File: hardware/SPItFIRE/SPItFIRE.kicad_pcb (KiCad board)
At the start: 2 copper layers, 114.3 x 83.8 mm, 45 parts, among them J1 Compact Host, J10 ISP, J11 Joystick A, J12 Joystick B, J13 Peripheral DE-9, J14 Peripheral User Port, J2 User Port Host, J3 User Port Passthrough, J4 SD Card Adapter, J5 DeadOnRTC, J6 SPI_4, J7 SPI_5, J8 SPI_6, J9 SPI_7, U1 74HC138, U2 ATmega1284P-A, Y1 Crystal

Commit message: Crystal load capacitors C2 and C6 are 0201 instead of 0603 and were missing their 27 pF values in the schematic
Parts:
- C2, C6: footprint Capacitor_SMD:C_0201_0603Metric_Pad0.64x0.40mm_HandSolder -> Capacitor_SMD:C_0603_1608Metric_Pad1.08x0.95mm_HandSolder
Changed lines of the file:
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@@
 		)
 	)
-	(footprint "Capacitor_SMD:C_0201_0603Metric_Pad0.64x0.40mm_HandSolder"
+	(footprint "Capacitor_SMD:C_0603_1608Metric_Pad1.08x0.95mm_HandSolder"
 		(layer "F.Cu")
 		(at 121.285 90.17)
-		(descr "Capacitor SMD 0201 (0603 Metric), square (rectangular) end terminal, IPC-7351 nominal with elongated pad for handsoldering. (Body size source: https://www.vishay.com/docs/20052/crcw0201e3.pdf)")
+		(descr "Capacitor SMD 0603 (1608 Metric), square (rectangular) end terminal, IPC-7351 nominal with elongated pad for handsoldering. (Body size source: IPC-SM-782 page 76, https://www.pcb-3d.com/wordpress/wp-content/uploads/ipc-sm-782a_amendment_1_and_2.pdf)")
 		(tags "capacitor handsolder")
 		(property "Reference" "C6"
-			(at 0 -1.05 0)
+			(at 2.667 0 0)
 			(layer "F.SilkS")
 			(effects
@@
 		)
 		(property "Value" "27pF"
-			(at 0 1.05 0)
+			(at 0 1.43 0)
 			(layer "F.Fab")
 			(effects
@@
 		(attr smd)
 		(duplicate_pad_numbers_are_jumpers no)
+		(fp_line
+			(start -0.146267 -0.51)
+			(end 0.146267 -0.51)
+			(stroke
+				(width 0.12)
+				(type solid)
+			)
+			(layer "F.SilkS")
+		)
+		(fp_line
+			(start -0.146267 0.51)
+			(end 0.146267 0.51)
+			(stroke
+				(width 0.12)
+				(type solid)
+			)
+			(layer "F.SilkS")
+		)
 		(fp_rect
-			(start -0.88 -0.35)
-			(end 0.88 0.35)
+			(start -1.65 -0.73)
+			(end 1.65 0.73)
 			(stroke
 				(width 0.05)
@@
 		)
 		(fp_rect
-			(start -0.3 -0.15)
-			(end 0.3 0.15)
+			(start -0.8 -0.4)
+			(end 0.8 0.4)
 			(stroke
 				(width 0.1)
@@
 		)
 		(fp_text user "${REFERENCE}"
-			(at 0 -0.68 0)
+			(at 0 0 0)
 			(layer "F.Fab")
 			(effects
 				(font
-					(size 0.25 0.25)
-					(thickness 0.04)
+					(size 0.4 0.4)
+					(thickness 0.06)
 				)
 			)
 		)
-		(pad "" smd roundrect
-			(at -0.4325 0)
-			(size 0.458 0.36)
-			(layers "F.Paste")
-			(roundrect_rratio 0.25)
-		)
-		(pad "" smd roundrect
-			(at 0.4325 0)
-			(size 0.458 0.36)
-			(layers "F.Paste")
-			(roundrect_rratio 0.25)
-		)
 		(pad "1" smd roundrect
-			(at -0.4075 0)
-			(size 0.635 0.4)
-			(layers "F.Cu" "F.Mask")
+			(at -0.8625 0)
+			(size 1.075 0.95)
+			(layers "F.Cu" "F.Mask" "F.Paste")
 			(roundrect_rratio 0.25)
 			(net "Net-(U2A-XTAL2)")
@@
 		)
 		(pad "2" smd roundrect
-			(at 0.4075 0)
-			(size 0.635 0.4)
-			(layers "F.Cu" "F.Mask")
+			(at 0.8625 0)
+			(size 1.075 0.95)
+			(layers "F.Cu" "F.Mask" "F.Paste")
 			(roundrect_rratio 0.25)
 			(net "GND")
@@
 		)
 		(embedded_fonts no)
-		(model "${KICAD10_3DMODEL_DIR}/Capacitor_SMD.3dshapes/C_0201_0603Metric.step"
+		(model "${KICAD10_3DMODEL_DIR}/Capacitor_SMD.3dshapes/C_0603_1608Metric.step"
 			(offset
 				(xyz 0 0 0)
@@
 		(tags "Through hole horizontal IDC header THT 2x10 2.54mm double row")
 		(property "Reference" "J14"
-			(at 7.145 -11.97 0)
+			(at -2.921 -10.414 0)
 			(layer "F.SilkS")
 			(effects
@@
 		)
 	)
-	(footprint "Capacitor_SMD:C_0201_0603Metric_Pad0.64x0.40mm_HandSolder"
+	(footprint "Capacitor_SMD:C_0603_1608Metric_Pad1.08x0.95mm_HandSolder"
 		(layer "F.Cu")
 		(at 121.285 97.79 180)
-		(descr "Capacitor SMD 0201 (0603 Metric), square (rectangular) end terminal, IPC-7351 nominal with elongated pad for handsoldering. (Body size source: https://www.vishay.com/docs/20052/crcw0201e3.pdf)")
+		(descr "Capacitor SMD 0603 (1608 Metric), square (rectangular) end terminal, IPC-7351 nominal with elongated pad for handsoldering. (Body size source: IPC-SM-782 page 76, https://www.pcb-3d.com/wordpress/wp-content/uploads/ipc-sm-782a_amendment_1_and_2.pdf)")
 		(tags "capacitor handsolder")
 		(property "Reference" "C2"
-			(at 0 -1.05 180)
+			(at 0 -1.43 180)
 			(layer "F.SilkS")
 			(effects
@@
 		)
 		(property "Value" "27pF"
-			(at 0 1.05 180)
+			(at 0 1.43 180)
 			(layer "F.Fab")
 			(effects
@@
 		(attr smd)
 		(duplicate_pad_numbers_are_jumpers no)
+		(fp_line
+			(start -0.146267 0.51)
+			(end 0.146267 0.51)
+			(stroke
+				(width 0.12)
+				(type solid)
+			)
+			(layer "F.SilkS")
+		)
+		(fp_line
+			(start -0.146267 -0.51)
+			(end 0.146267 -0.51)
+			(stroke
+				(width 0.12)
+				(type solid)
+			)
+			(layer "F.SilkS")
+		)
 		(fp_rect
-			(start -0.88 -0.35)
-			(end 0.88 0.35)
+			(start -1.65 -0.73)
+			(end 1.65 0.73)
 			(stroke
 				(width 0.05)
@@
 		)
 		(fp_rect
-			(start -0.3 -0.15)
-			(end 0.3 0.15)
+			(start -0.8 -0.4)
+			(end 0.8 0.4)
 			(stroke
 				(width 0.1)
@@
 		)
 		(fp_text user "${REFERENCE}"
-			(at 0 -0.68 180)
+			(at 0 0 180)
 			(layer "F.Fab")
 			(effects
 				(font
-					(size 0.25 0.25)
-					(thickness 0.04)
+					(size 0.4 0.4)
+					(thickness 0.06)
 				)
 			)
 		)
-		(pad "" smd roundrect
-			(at -0.4325 0 180)
-			(size 0.458 0.36)
-			(layers "F.Paste")
-			(roundrect_rratio 0.25)
-		)
-		(pad "" smd roundrect
-			(at 0.4325 0 180)
-			(size 0.458 0.36)
-			(layers "F.Paste")
-			(roundrect_rratio 0.25)
-		)
 		(pad "1" smd roundrect
-			(at -0.4075 0 180)
-			(size 0.635 0.4)
-			(layers "F.Cu" "F.Mask")
+			(at -0.8625 0 180)
+			(size 1.075 0.95)
+			(layers "F.Cu" "F.Mask" "F.Paste")
 			(roundrect_rratio 0.25)
 			(net "Net-(U2A-XTAL1)")
@@
 		)
 		(pad "2" smd roundrect
-			(at 0.4075 0 180)
-			(size 0.635 0.4)
-			(layers "F.Cu" "F.Mask")
+			(at 0.8625 0 180)
+			(size 1.075 0.95)
+			(layers "F.Cu" "F.Mask" "F.Paste")
 			(roundrect_rratio 0.25)
 			(net "GND")
@@
 		)
 		(embedded_fonts no)
-		(model "${KICAD10_3DMODEL_DIR}/Capacitor_SMD.3dshapes/C_0201_0603Metric.step"
+		(model "${KICAD10_3DMODEL_DIR}/Capacitor_SMD.3dshapes/C_0603_1608Metric.step"
 			(offset
 				(xyz 0 0 0)
@@
 		(tags "resistor handsolder")
 		(property "Reference" "R2"
-			(at 0 1.397 270)
+			(at 0 1.905 0)
 			(layer "F.SilkS")
 			(effects
@@
 		(tags "capacitor handsolder")
 		(property "Reference" "C5"
-			(at 2.54 -1.27 0)
+			(at 2.413 -0.127 90)
 			(layer "F.SilkS")
 			(effects
@@
 	)
 	(segment
+		(start 122.1475 89.99)
+		(end 120.4225 88.265)
+		(width 0.2)
+		(layer "F.Cu")
+		(net "GND")
+	)
+	(segment
 		(start 168.91 78.74)
 		(end 162.56 78.74)
@@
 	)
 	(segment
+		(start 122.1475 90.17)
+		(end 122.1475 89.99)
+		(width 0.2)
+		(layer "F.Cu")
+		(net "GND")
+	)
+	(segment
 		(start 130.175 53.34)
 		(end 154.94 53.34)
@@
 	)
 	(segment
-		(start 120.4225 89.3075)
-		(end 120.65 89.535)
-		(width 0.2)
-		(layer "F.Cu")
-		(net "GND")
-	)
-	(segment
 		(start 140.97 58.42)
 		(end 139.7 57.15)
@@
 	)
 	(segment
-		(start 121.6925 89.9425)
-		(end 121.285 89.535)
-		(width 0.2)
-		(layer "F.Cu")
-		(net "GND")
-	)
-	(segment
 		(start 74.93 105.41)
 		(end 76.2 106.68)
@@
 	)
 	(segment
-		(start 120.4225 88.265)
-		(end 120.4225 89.3075)
-		(width 0.2)
-		(layer "F.Cu")
-		(net "GND")
-	)
-	(segment
 		(start 142.24 68.58)
 		(end 142.24 64.320635)
@@
 		(width 0.2)
 		(layer "F.Cu")
-		(net "GND")
-	)
-	(segment
-		(start 121.285 89.535)
-		(end 120.65 89.535)
-		(width 0.2)
-		(layer "F.Cu")

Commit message: Adds weak pull-ups to the address lines to give them definite state when the Compact is not connected
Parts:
- added R10: 100K, Resistor_SMD:R_0603_1608Metric_Pad0.98x0.95mm_HandSolder, F.Cu at (82.3, 59.2)
- added R8: 100K, Resistor_SMD:R_0603_1608Metric_Pad0.98x0.95mm_HandSolder, F.Cu at (78.0, 59.2)
- added R9: 100K, Resistor_SMD:R_0603_1608Metric_Pad0.98x0.95mm_HandSolder, F.Cu at (86.9, 59.2)
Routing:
- net +5V: track 574.2 -> 596.6 mm
- net /main/A2: track 90.0 -> 105.0 mm, vias 1 -> 2
- net GND: track 827.5 -> 820.2 mm
- net /main/A1: track 80.8 -> 84.5 mm
- net /main/A0: track 86.0 -> 89.2 mm
- net SCK: track 291.0 -> 292.5 mm

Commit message: Fixed the footprint of C3
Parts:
- C3: footprint LED_SMD:LED_0603_1608Metric_Pad1.05x0.95mm_HandSolder -> Capacitor_SMD:C_0603_1608Metric_Pad1.08x0.95mm_HandSolder
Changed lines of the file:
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@@
 		)
 	)
-	(footprint "LED_SMD:LED_0603_1608Metric_Pad1.05x0.95mm_HandSolder"
+	(footprint "Capacitor_SMD:C_0603_1608Metric_Pad1.08x0.95mm_HandSolder"
 		(layer "F.Cu")
 		(at 132.715 80.645 180)
-		(descr "LED SMD 0603 (1608 Metric), square (rectangular) end terminal, IPC-7351 nominal, (Body size source: http://www.tortai-tech.com/upload/download/2011102023233369053.pdf)")
-		(tags "LED handsolder")
+		(descr "Capacitor SMD 0603 (1608 Metric), square (rectangular) end terminal, IPC-7351 nominal with elongated pad for handsoldering. (Body size source: IPC-SM-782 page 76, https://www.pcb-3d.com/wordpress/wp-content/uploads/ipc-sm-782a_amendment_1_and_2.pdf)")
+		(tags "capacitor handsolder")
 		(property "Reference" "C3"
-			(at 0 1.905 0)
+			(at -0.033767 1.397 180)
 			(layer "F.SilkS")
 			(effects
@@
 		)
 		(property "Value" "10uF"
-			(at -3.81 0 0)
+			(at 0 1.43 180)
 			(layer "F.Fab")
 			(effects
@@
 		)
 		(property "Datasheet" ""
-			(at 0 0 0)
+			(at 0 0 180)
 			(layer "F.Fab")
 			(hide yes)
@@
 		)
 		(property "Description" "Unpolarized capacitor"
-			(at 0 0 0)
+			(at 0 0 180)
 			(layer "F.Fab")
 			(hide yes)
@@
 		)
 		(property "KiLib_Generator" "SMD_2terminal_chip_molded"
-			(at 0 0 0)
+			(at 0 0 180)
 			(layer "F.SilkS")
 			(hide yes)
@@
 		(duplicate_pad_numbers_are_jumpers no)
 		(fp_line
-			(start 0.8 -0.735)
-			(end -1.66 -0.735)
-			(stroke
-				(width 0.12)
-				(type solid)
-			)
-			(layer "F.SilkS")
-		)
-		(fp_line
-			(start -1.66 0.735)
-			(end 0.8 0.735)
+			(start -0.146267 0.51)
+			(end 0.146267 0.51)
 			(stroke
 				(width 0.12)
@@
 		)
 		(fp_line
-			(start -1.66 -0.735)
-			(end -1.66 0.735)
+			(start -0.146267 -0.51)
+			(end 0.146267 -0.51)
 			(stroke
 				(width 0.12)
@@
 			(layer "F.CrtYd")
 		)
-		(fp_line
-			(start 0.8 0.4)
-			(end 0.8 -0.4)
-			(stroke
-				(width 0.1)
-				(type solid)
-			)
-			(layer "F.Fab")
-		)
-		(fp_line
-			(start 0.8 -0.4)
-			(end -0.5 -0.4)
-			(stroke
-				(width 0.1)
-				(type solid)
-			)
-			(layer "F.Fab")
-		)
-		(fp_line
-			(start -0.5 -0.4)
-			(end -0.8 -0.1)
-			(stroke
-				(width 0.1)
-				(type solid)
-			)
-			(layer "F.Fab")
-		)
-		(fp_line
-			(start -0.8 0.4)
+		(fp_rect
+			(start -0.8 -0.4)
 			(end 0.8 0.4)
 			(stroke
@@
 				(type solid)
 			)
-			(layer "F.Fab")
-		)
-		(fp_line
-			(start -0.8 -0.1)
-			(end -0.8 0.4)
-			(stroke
-				(width 0.1)
-				(type solid)
-			)
+			(fill no)
 			(layer "F.Fab")
 		)
 		(fp_text user "${REFERENCE}"
-			(at 0 0 0)
+			(at 0 0 180)
 			(layer "F.Fab")
 			(effects
@@
 		)
 		(pad "1" smd roundrect
-			(at -0.875 0 180)
-			(size 1.05 0.95)
+			(at -0.8625 0 180)
+			(size 1.075 0.95)
 			(layers "F.Cu" "F.Mask" "F.Paste")
 			(roundrect_rratio 0.25)
@@
 		)
 		(pad "2" smd roundrect
-			(at 0.875 0 180)
-			(size 1.05 0.95)
+			(at 0.8625 0 180)
+			(size 1.075 0.95)
 			(layers "F.Cu" "F.Mask" "F.Paste")
 			(roundrect_rratio 0.25)
@@
 		)
 		(embedded_fonts no)
-		(model "${KICAD10_3DMODEL_DIR}/LED_SMD.3dshapes/LED_0603_1608Metric.step"
+		(model "${KICAD10_3DMODEL_DIR}/Capacitor_SMD.3dshapes/C_0603_1608Metric.step"
 			(offset
 				(xyz 0 0 0)
@@
 		(tags "resistor handsolder")
 		(property "Reference" "R1"
-			(at 0 -1.43 90)
+			(at 2.4395 0.127 180)
 			(layer "F.SilkS")
 			(effects
@@
 		(tags "capacitor handsolder")
 		(property "Reference" "C4"
-			(at -2.3125 0 180)
+			(at -2.4395 0 180)
 			(layer "F.SilkS")
 			(effects

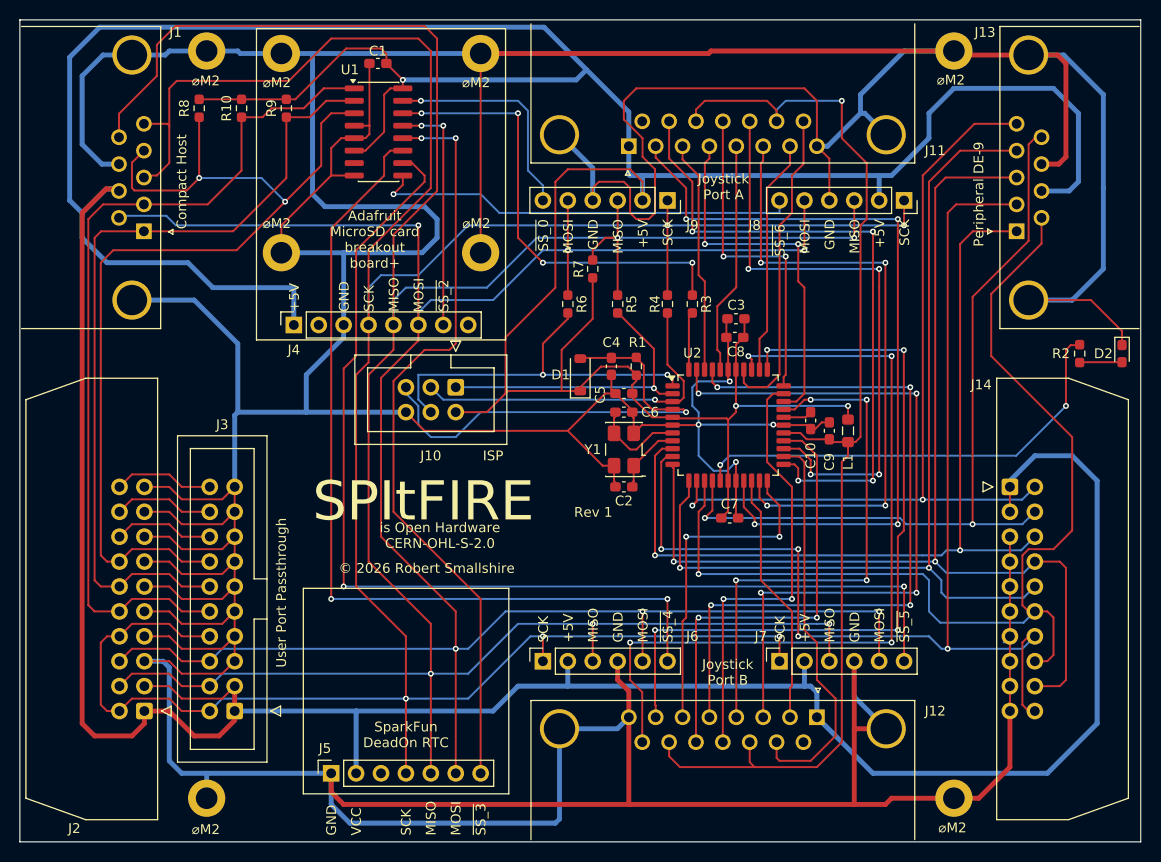
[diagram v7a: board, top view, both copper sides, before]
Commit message: Front and back ground pours
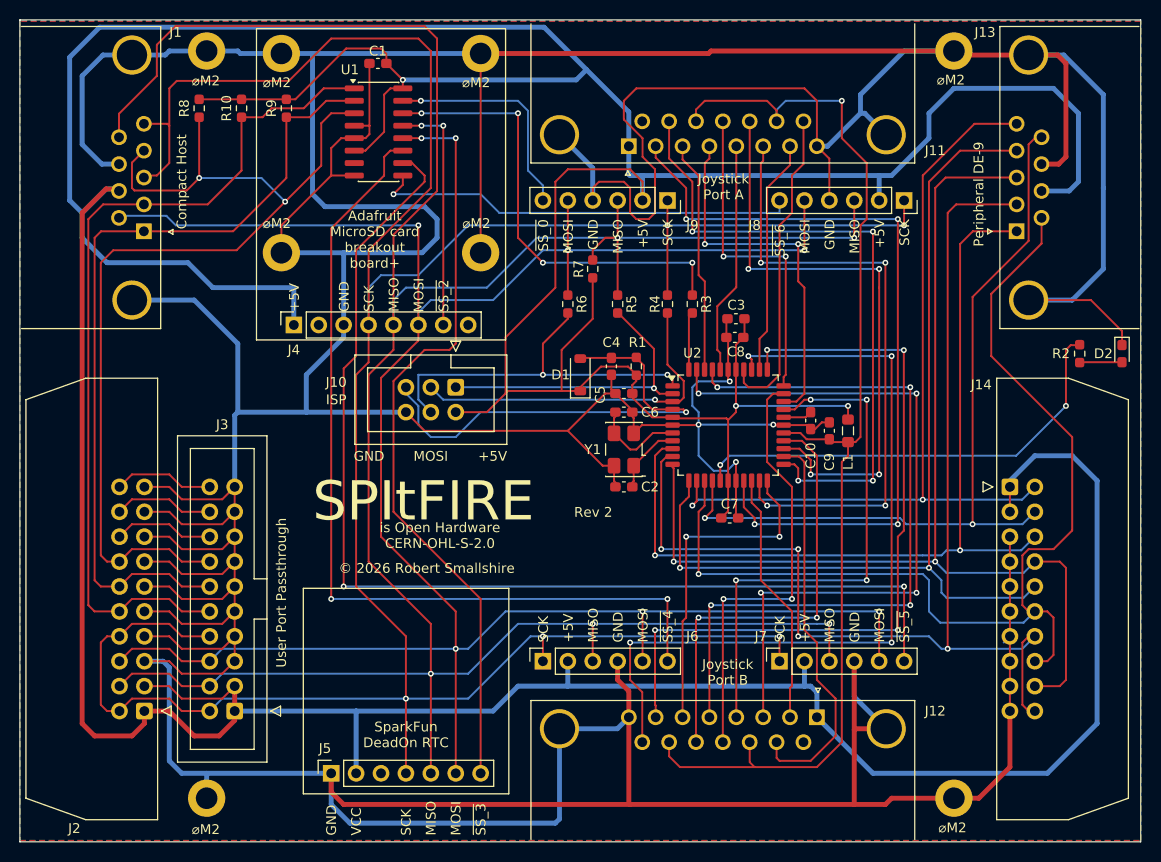
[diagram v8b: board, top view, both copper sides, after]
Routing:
- added copper zone on B.Cu, net GND
- added copper zone on F.Cu, net GND
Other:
- board text added: "Rev 2"
- board text removed: "Rev 1"
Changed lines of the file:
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@@
 		(tags "capacitor handsolder")
 		(property "Reference" "C2"
-			(at 0 -1.43 180)
+			(at -2.667 0 180)
 			(layer "F.SilkS")
 			(effects
@@
 		)
 		(property "Value" "ISP"
-			(at 6.985 -3.81 180)
+			(at 1.27 12.192 180)
 			(layer "F.SilkS")
 			(effects
@@
 		)
 		(fp_text user "${REFERENCE}"
-			(at 6.985 2.54 0)
+			(at -0.508 12.192 0)
 			(layer "F.SilkS")
 			(effects
@@
 		)
 	)
+	(gr_text "GND"
+		(at 93.726 95.25 0)
+		(layer "F.SilkS")
+		(effects
+			(font
+				(size 1 1)
+				(thickness 0.1)
+			)
+			(justify left bottom)
+		)
+	)
+	(gr_text "MOSI"
+		(at 99.822 95.25 0)
+		(layer "F.SilkS")
+		(effects
+			(font
+				(size 1 1)
+				(thickness 0.1)
+			)
+			(justify left bottom)
+		)
+	)
 	(gr_text "⌀M2"
 		(at 104.775 57.15 0)
@@
 		)
 	)
-	(gr_text "Rev 1"
+	(gr_text "+5V"
+		(at 106.426 95.25 0)
+		(layer "F.SilkS")
+		(effects
+			(font
+				(size 1 1)
+				(thickness 0.1)
+			)
+			(justify left bottom)
+		)
+	)
+	(gr_text "Rev 2"
 		(at 116.205 100.965 0)
 		(layer "F.SilkS")
@@
 		(net "~{SS_0}")
 	)
+	(zone
+		(net "GND")
+		(layer "F.Cu")
+		(name "f.gnd")
+		(hatch edge 0.5)
+		(priority 1)
+		(connect_pads
+			(clearance 0.5)
+		)
+		(min_thickness 0.25)
+		(fill yes
+			(thermal_gap 0.5)
+			(thermal_bridge_width 0.5)
+			(island_removal_mode 0)
+		)
+		(polygon
+			(pts
+				(xy 59.69 50.292) (xy 59.69 133.858) (xy 173.99 133.858) (xy 173.99 50.292)
+			)
+		)
+	)
+	(zone
+		(net "GND")
+		(layer "B.Cu")
+		(name "b.gnd")
+		(hatch edge 0.5)
+		(connect_pads
+			(clearance 0.5)
+		)
+		(min_thickness 0.25)
+		(fill yes
+			(thermal_gap 0.5)
+			(thermal_bridge_width 0.5)
+			(island_removal_mode 0)
+		)
+		(polygon
+			(pts
+				(xy 59.69 50.292) (xy 59.69 133.858) (xy 173.99 133.858) (xy 173.99 50.292)
+			)
+		)
+	)
 	(group ""
